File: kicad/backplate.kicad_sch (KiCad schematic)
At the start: 3 parts, among them J1 10018784-10210TLF

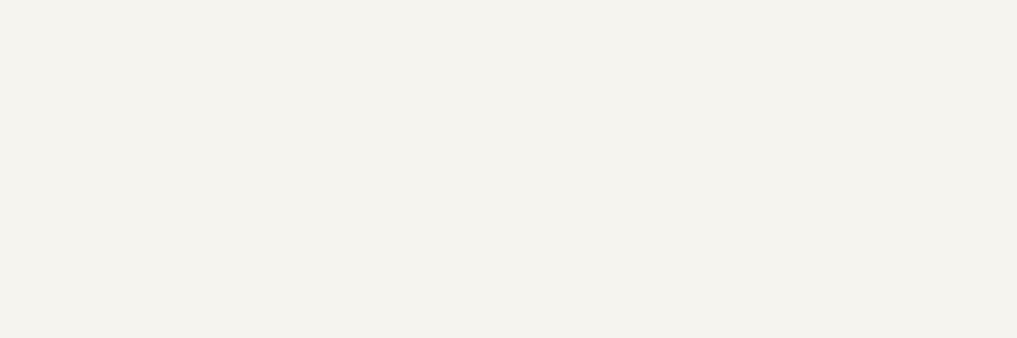
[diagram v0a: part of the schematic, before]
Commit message: add title to schematic
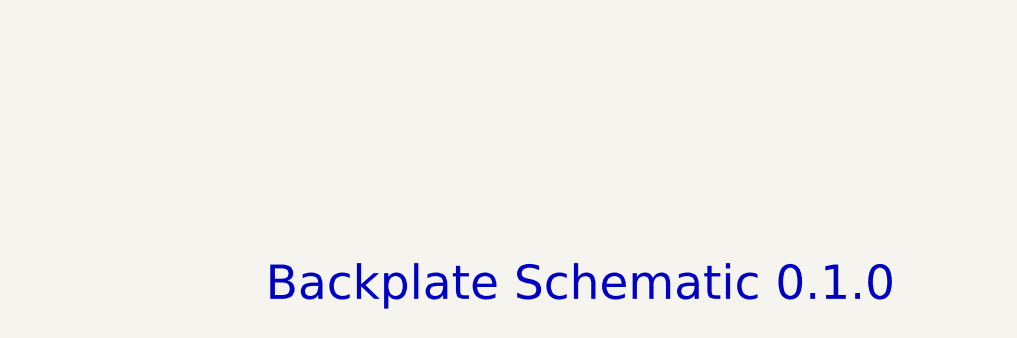
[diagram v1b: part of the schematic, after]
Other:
- note added: "Backplate Schematic 0.1.0"
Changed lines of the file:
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@@
+		)
+	)
+	(text "Backplate Schematic 0.1.0"
+		(exclude_from_sim no)
+		(at 223.774 173.99 0)
+		(effects
+			(font
+				(size 3.81 3.81)
+			)
 		)
 	)
